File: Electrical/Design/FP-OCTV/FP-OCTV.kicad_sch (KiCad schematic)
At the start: 31 parts

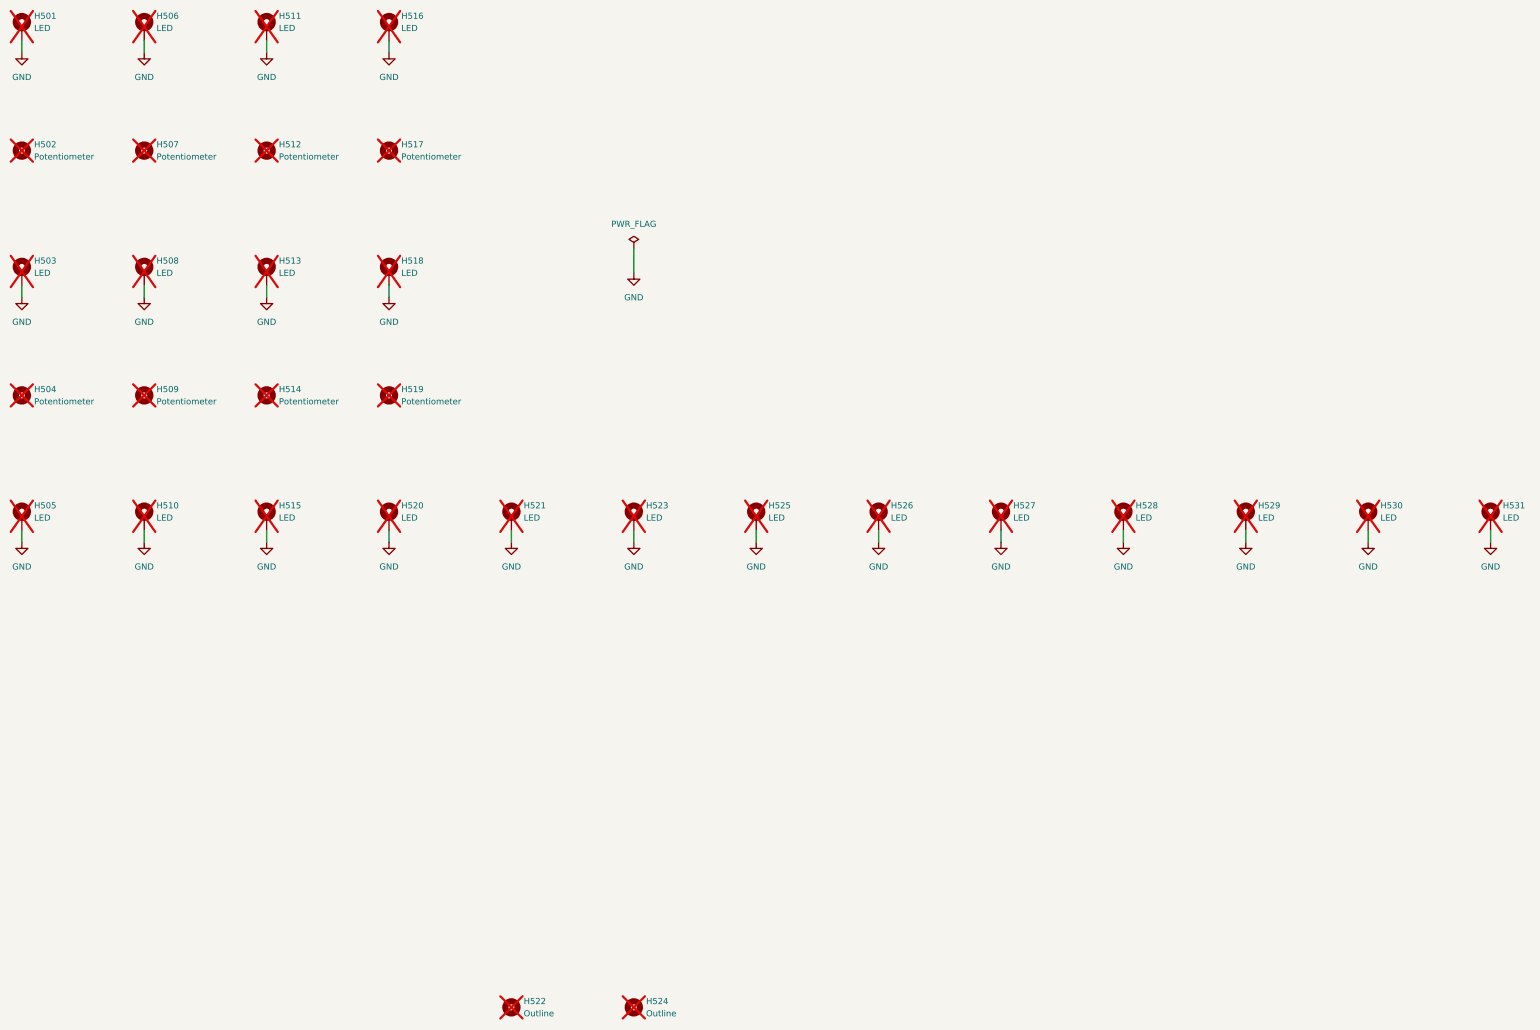
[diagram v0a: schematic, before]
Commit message: SUKU octv buttons rotated, spacers updated
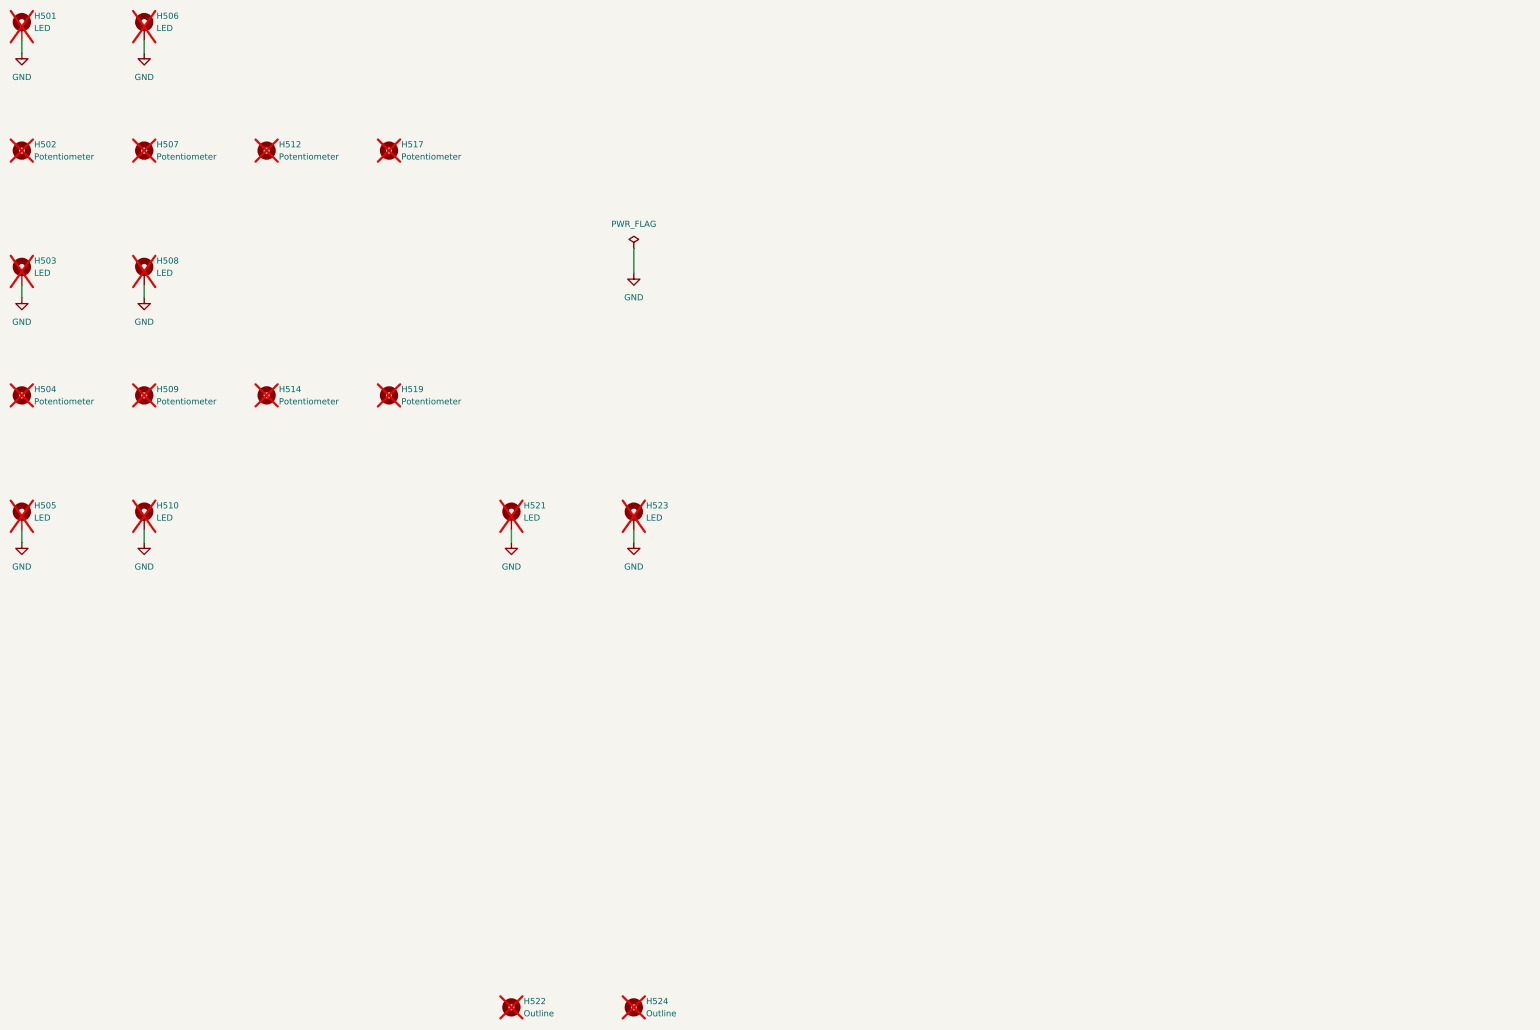
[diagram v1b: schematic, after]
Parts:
- removed H511, H513, H515, H516, H518, H520, H525, H526, H527, H528, H529, H530, H531: LED, suku_basics:FP_LED_TIGHT, symbol Mechanical:MountingHole_Pad
